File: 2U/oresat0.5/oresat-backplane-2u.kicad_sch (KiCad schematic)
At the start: 59 parts, among them J1 m55-6001642

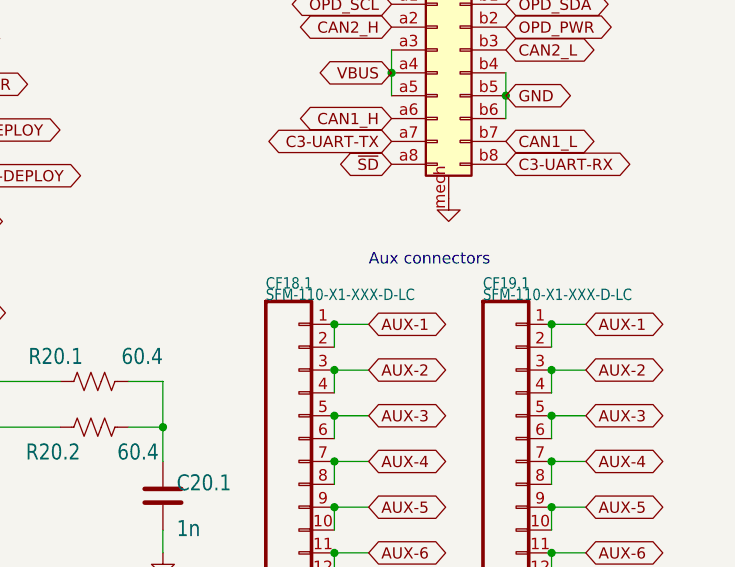
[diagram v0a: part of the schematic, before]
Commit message: Moved aux connectors, fixed RF connector soldermask
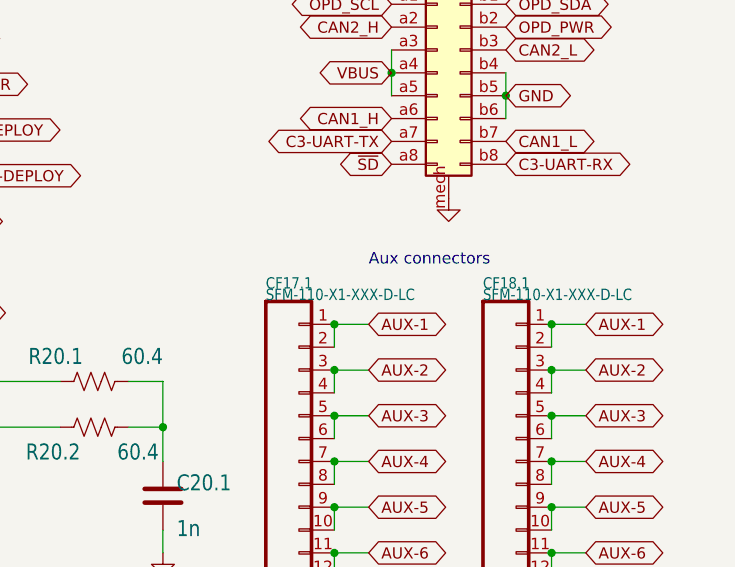
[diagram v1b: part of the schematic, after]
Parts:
- renumbered CF18.1 to CF17.1, CF19.1 to CF18.1
